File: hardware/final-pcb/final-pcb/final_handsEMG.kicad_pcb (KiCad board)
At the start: 2 copper layers, 192 parts, among them J1 Conn_02x13_Odd_Even, U1 ADS1299CPAG, U2 STM32L496ZGT6, U3 FT231XQ-R, U6 TPS60403DBVT, U8 TPS72325DBVT, U9 TPS73225DBVT

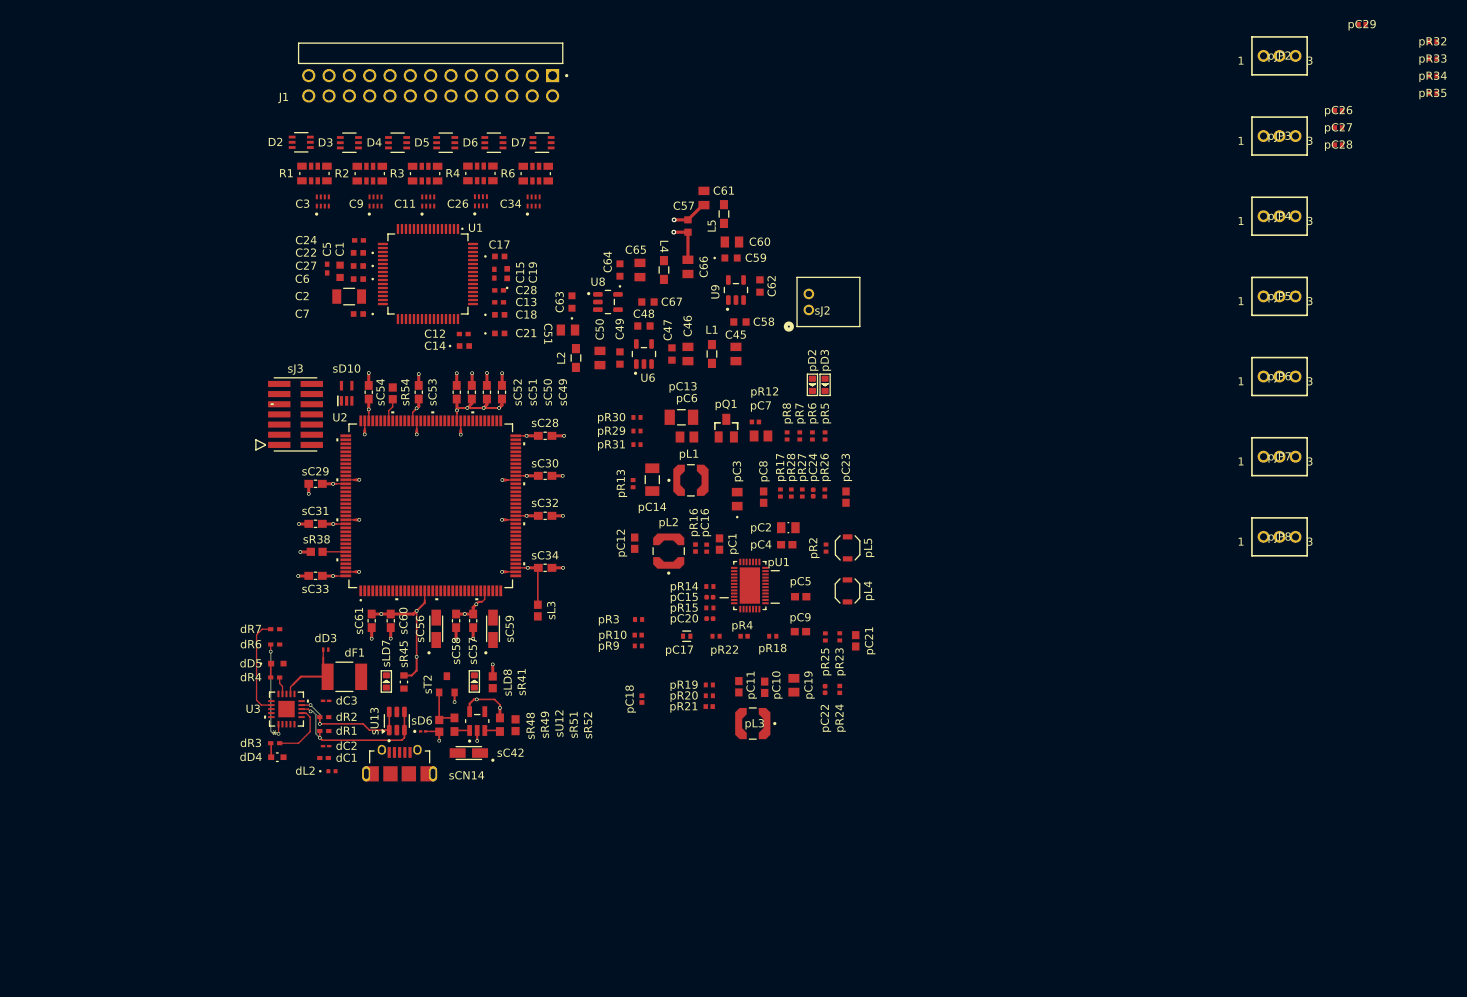
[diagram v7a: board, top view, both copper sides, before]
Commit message: Everything organized and ready to position and route
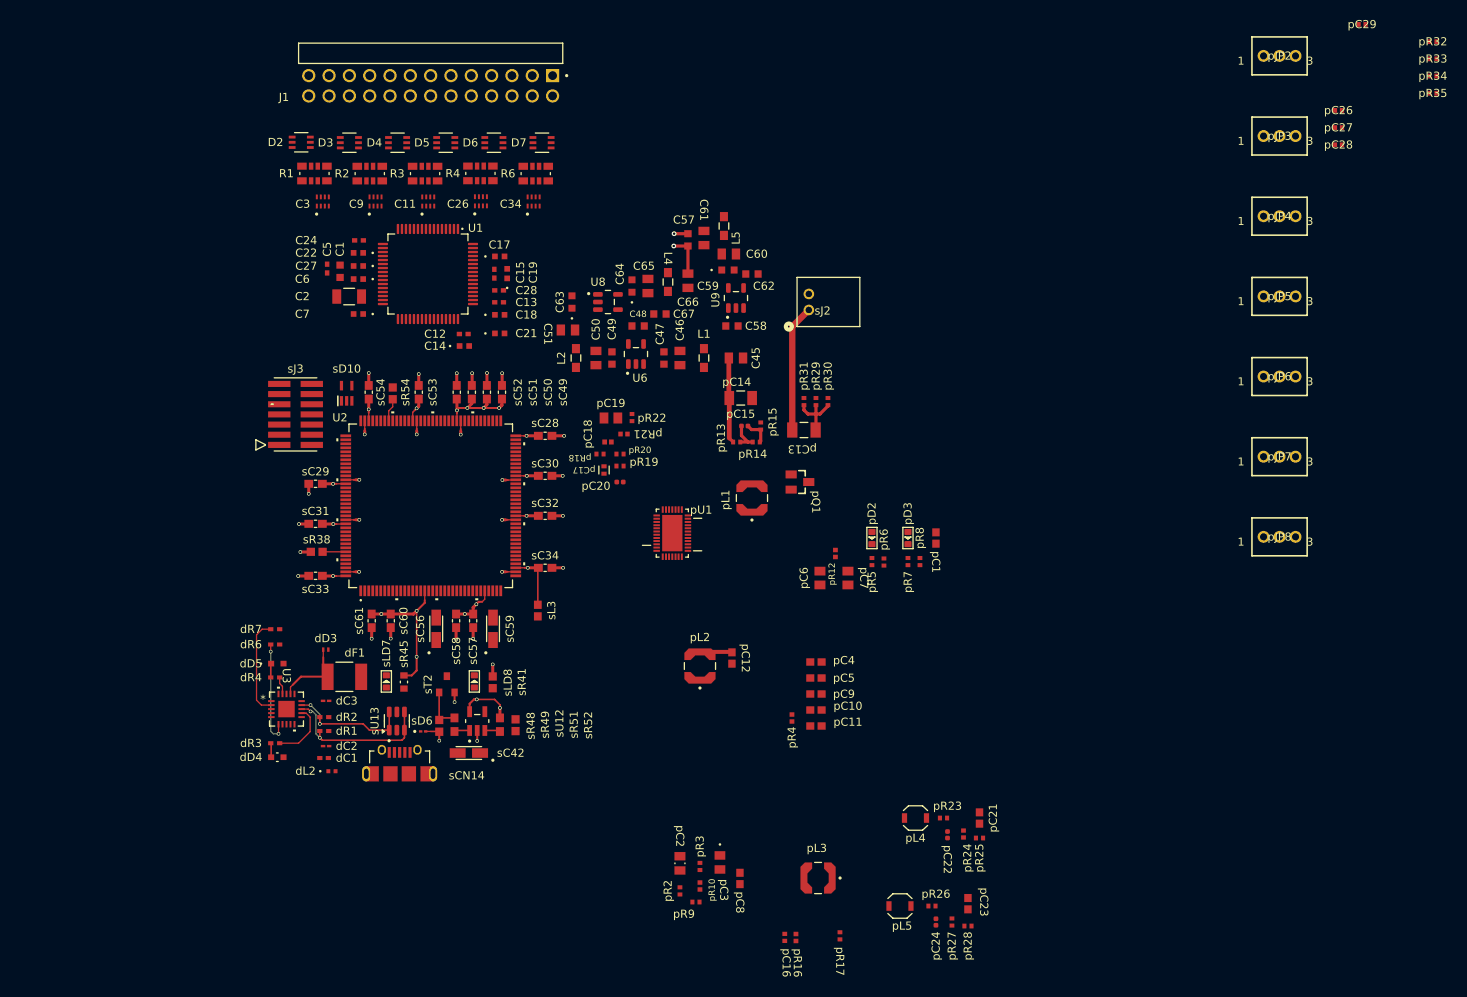
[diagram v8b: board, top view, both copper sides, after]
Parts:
- moved pR28 58.5 mm to (173.0, 142.5), turned to 0 degrees
- moved pR27 56.8 mm to (171.0, 142.0)
- moved pR17 55.8 mm to (157.0, 143.7), turned to -90 degrees
- moved pC24 55.8 mm to (169.0, 142.0)
- moved pR26 53.3 mm to (168.5, 140.0), turned to 0 degrees
- moved pC23 53.1 mm to (173.0, 139.7), turned to 90 degrees
- moved pR16 50.3 mm to (151.5, 143.9), turned to -90 degrees
- moved pC16 49.6 mm to (150.1, 143.9), turned to -90 degrees
- moved pC8 47.8 mm to (144.5, 136.6), turned to -90 degrees
- moved pR2 46.6 mm to (137.0, 138.1)
- moved pC3 45.5 mm to (142.0, 134.6), turned to -90 degrees
- moved pL5 45.2 mm to (164.5, 140.0), turned to 0 degrees
- moved pC2 44.1 mm to (137.0, 134.7), turned to -90 degrees
- moved pC19 40.5 mm to (128.4, 79.0), turned to 0 degrees
- moved pR21 35.7 mm to (130.0, 81.0)
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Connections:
- pD2 pad +: (no net) -> LDO3V3
- pD2 pad -: (no net) -> Net-(pD2-K)
- pD3 pad +: (no net) -> LDO3V3
- pD3 pad -: (no net) -> Net-(pD3-K)
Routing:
- net BAT: track 0.00 -> 15.9 mm
- net 5VCC: track 0.00 -> 10.7 mm
- net Net-(pC13-Pad2): track 0.00 -> 7.47 mm
- net PVIN3: track 0.00 -> 4.02 mm
- net Net-(pC15-Pad1): track 0.00 -> 3.89 mm
- net FB4: track 0.00 -> 3.38 mm
- net AVDD: track 10.4 -> 7.64 mm
